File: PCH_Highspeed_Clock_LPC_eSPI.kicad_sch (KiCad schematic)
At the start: 1 part

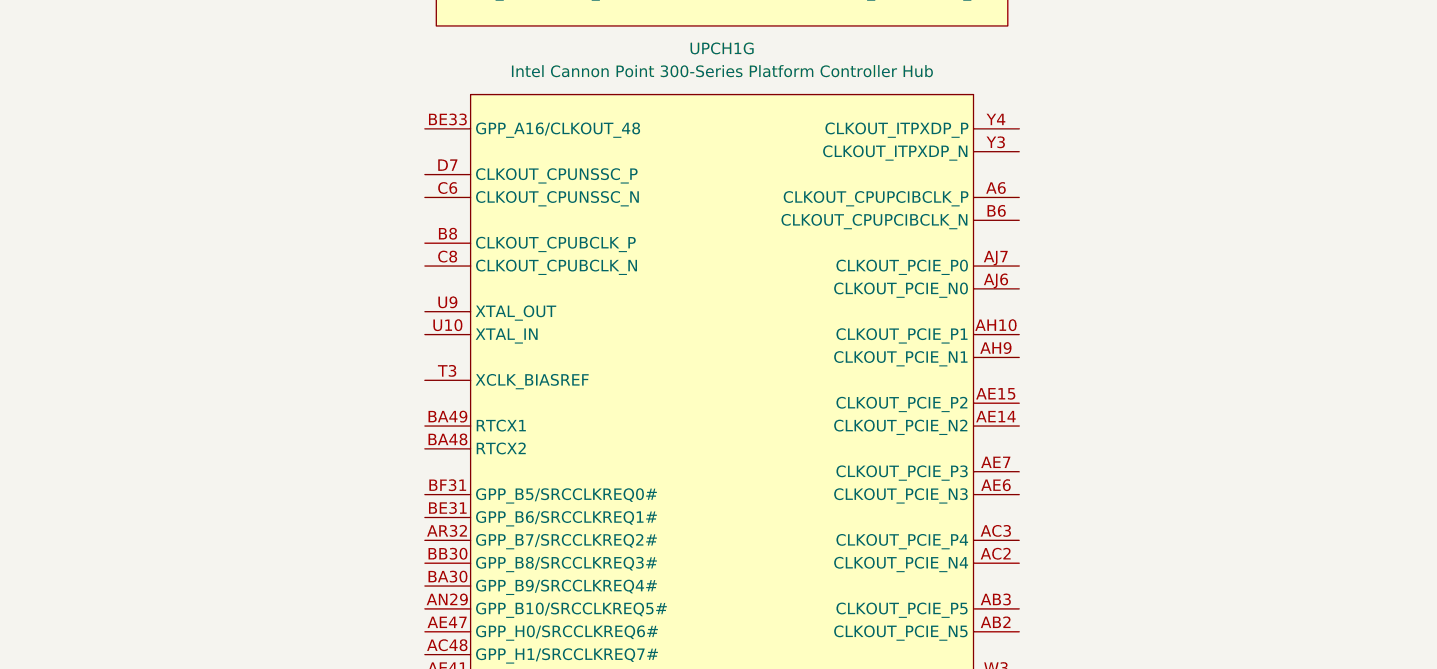
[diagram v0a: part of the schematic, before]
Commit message: Added pcie slot and cpu clocks
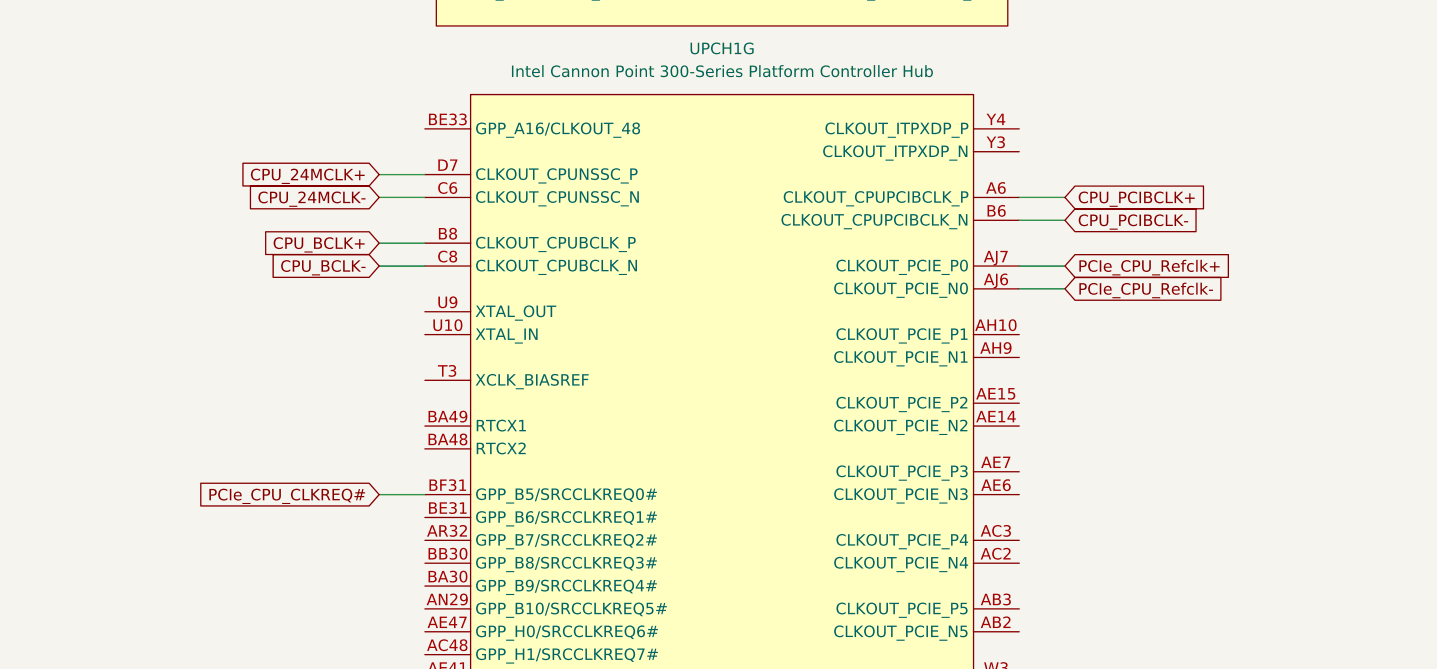
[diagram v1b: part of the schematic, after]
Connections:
- net CPU_PCIBCLK+: now reaches UPCH1.A6 (CLKOUT_CPUPCIBCLK_P)
- net PCIe_CPU_Refclk-: now reaches UPCH1.AJ6 (CLKOUT_PCIE_N0)
- net PCIe_CPU_Refclk+: now reaches UPCH1.AJ7 (CLKOUT_PCIE_P0)
- net CPU_PCIBCLK-: now reaches UPCH1.B6 (CLKOUT_CPUPCIBCLK_N)
- net CPU_BCLK+: now reaches UPCH1.B8 (CLKOUT_CPUBCLK_P)
- net PCIe_CPU_CLKREQ#: now reaches UPCH1.BF31 (GPP_B5/SRCCLKREQ0#)
- net CPU_24MCLK-: now reaches UPCH1.C6 (CLKOUT_CPUNSSC_N)
- net CPU_BCLK-: now reaches UPCH1.C8 (CLKOUT_CPUBCLK_N)
- net CPU_24MCLK+: now reaches UPCH1.D7 (CLKOUT_CPUNSSC_P)

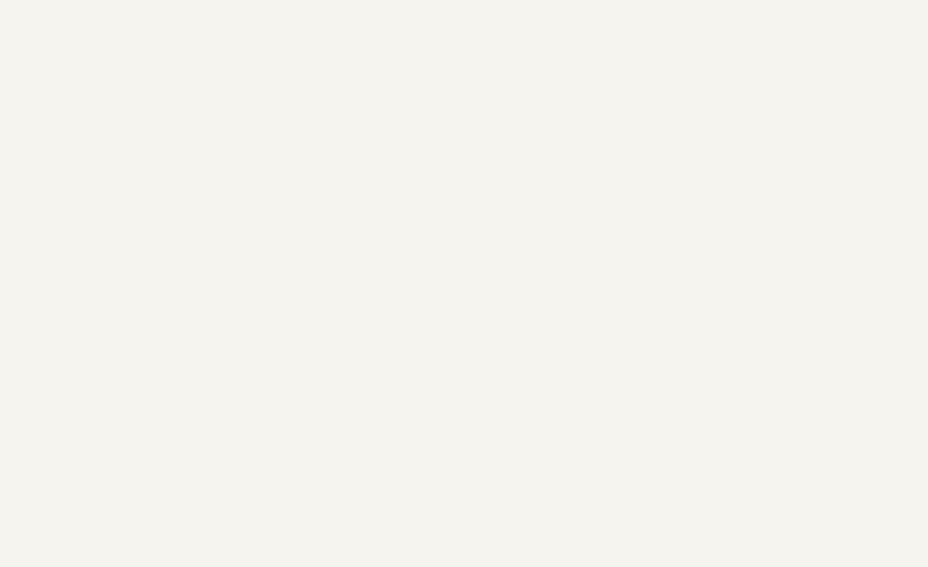
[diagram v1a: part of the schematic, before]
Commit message: Added PCH SKU IO table screenshot from datasheet to schematic
and a note about display audio
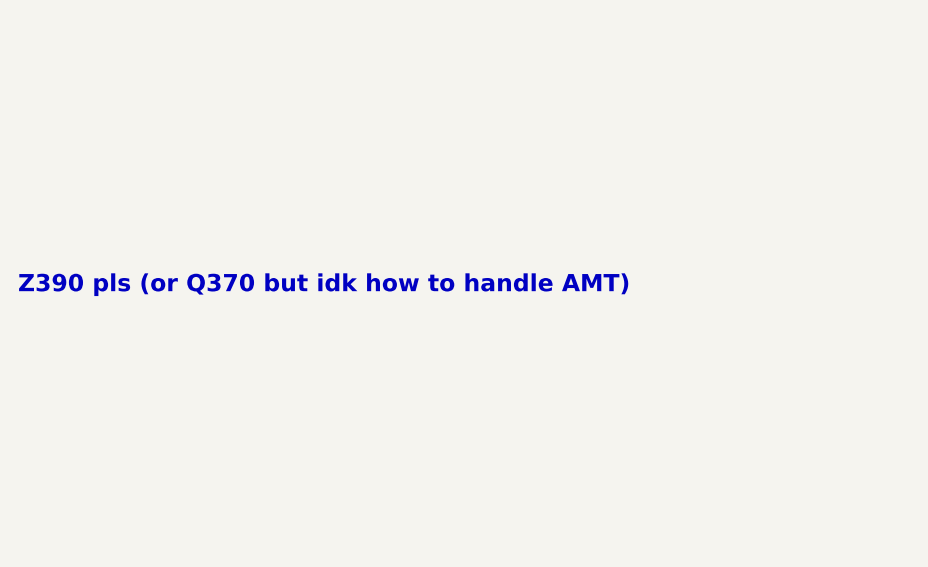
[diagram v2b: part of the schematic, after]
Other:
- note added: "Z390 pls (or Q370 but idk how to handle AMT)"

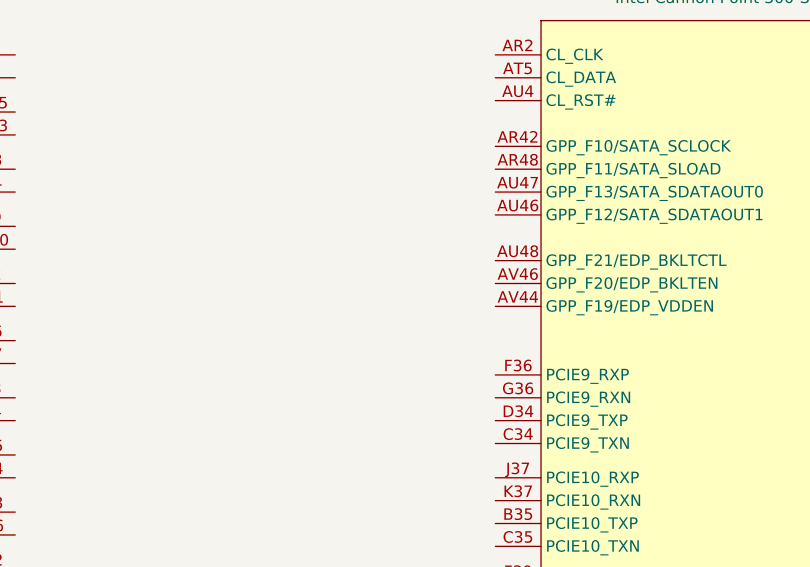
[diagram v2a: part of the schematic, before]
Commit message: partially added eDP + rearranged other display stuff
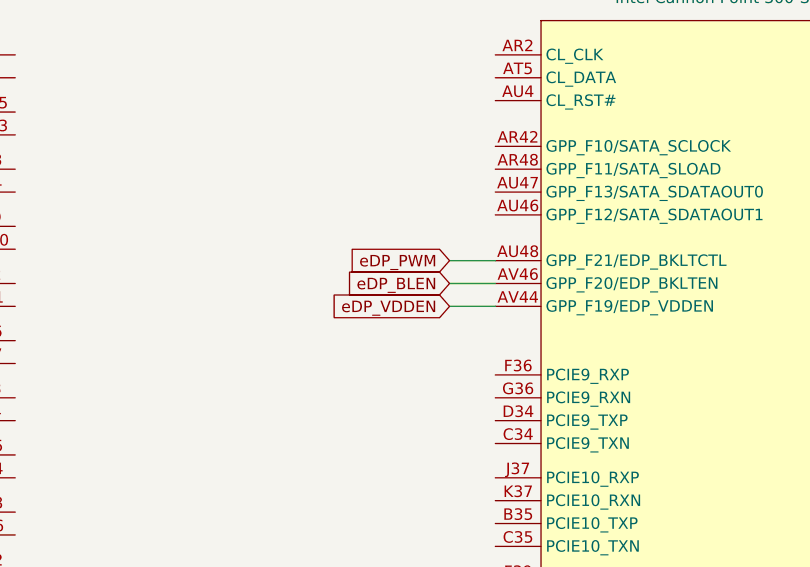
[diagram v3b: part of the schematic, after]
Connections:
- net eDP_PWM: now reaches UPCH1.AU48 (GPP_F21/EDP_BKLTCTL)
- net eDP_VDDEN: now reaches UPCH1.AV44 (GPP_F19/EDP_VDDEN)
- net eDP_BLEN: now reaches UPCH1.AV46 (GPP_F20/EDP_BKLTEN)
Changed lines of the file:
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@@
+	(wire
+		(pts
+			(xy 180.34 57.15) (xy 185.42 57.15)
+		)
+		(stroke
+			(width 0)
+			(type default)
+		)
+	)
 	(wire
 		(pts
@@
 	(wire
 		(pts
-			(xy 54.61 57.15) (xy 58.42 57.15)
+			(xy 180.34 52.07) (xy 185.42 52.07)
 		)
 		(stroke
@@
 	(wire
 		(pts
-			(xy 54.61 64.77) (xy 58.42 64.77)
+			(xy 54.61 57.15) (xy 58.42 57.15)
 		)
 		(stroke
@@
 	(wire
 		(pts
-			(xy 260.35 176.53) (xy 255.27 176.53)
+			(xy 54.61 64.77) (xy 58.42 64.77)
 		)
 		(stroke
@@
 	(wire
 		(pts
+			(xy 260.35 176.53) (xy 255.27 176.53)
+		)
+		(stroke
+			(width 0)
+			(type default)
+		)
+	)
+	(wire
+		(pts
 			(xy 184.15 176.53) (xy 189.23 176.53)
+		)
+		(stroke
+			(width 0)
+			(type default)
+		)
+	)
+	(wire
+		(pts
+			(xy 180.34 54.61) (xy 185.42 54.61)
 		)
 		(stroke
@@
 		)
 	)
+	(global_label "eDP_VDDEN"
+		(shape input)
+		(at 180.34 57.15 180)
+		(fields_autoplaced yes)
+		(effects
+			(font
+				(size 1.27 1.27)
+			)
+			(justify right)
+		)
+		(property "Intersheetrefs" "${INTERSHEET_REFS}"
+			(at 159.8771 57.15 0)
+			(effects
+				(font
+					(size 1.27 1.27)
+				)
+				(justify right)
+				(hide yes)
+			)
+		)
+	)
 	(global_label "DMI_CRx_PTx_2+"
 		(shape input)
@@
 		)
 	)
+	(global_label "eDP_PWM"
+		(shape input)
+		(at 180.34 52.07 180)
+		(fields_autoplaced yes)
+		(effects
+			(font
+				(size 1.27 1.27)
+			)
+			(justify right)
+		)
+		(property "Intersheetrefs" "${INTERSHEET_REFS}"
+			(at 159.8771 52.07 0)
+			(effects
+				(font
+					(size 1.27 1.27)
+				)
+				(justify right)
+				(hide yes)
+			)
+		)
+	)
 	(global_label "DMI_CTx_PRx_2+"
 		(shape input)
@@
 			(effects
 				(font
+					(size 1.27 1.27)
+				)
+				(justify right)
+				(hide yes)
+			)
+		)
+	)
+	(global_label "eDP_BLEN"
+		(shape input)
+		(at 180.34 54.61 180)
+		(fields_autoplaced yes)
+		(effects
+			(font
+				(size 1.27 1.27)
+			)
+			(justify right)
+		)
+		(property "Intersheetrefs" "${INTERSHEET_REFS}"
+			(at 159.8771 54.61 0)
+			(effects
+				(font

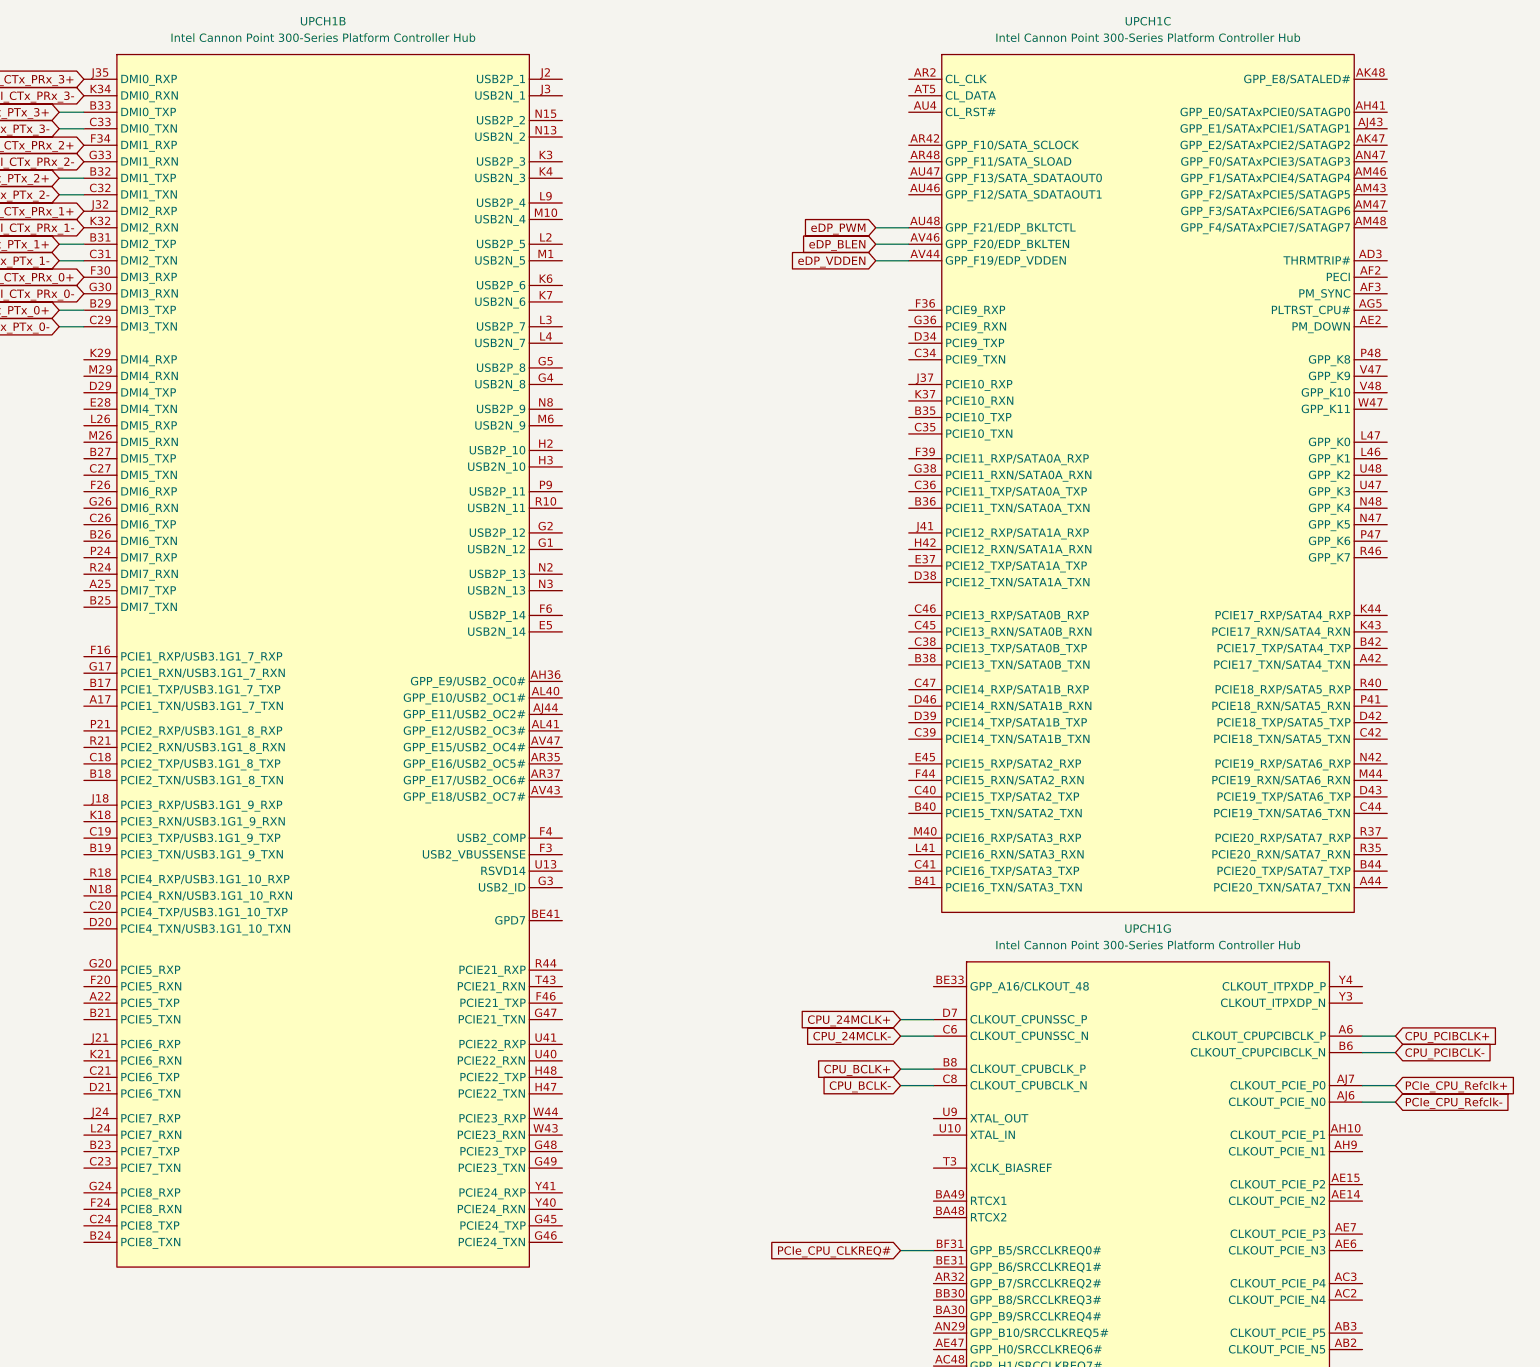
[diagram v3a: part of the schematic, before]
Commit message: Added PCH PCIe rootport/bifurcation notes
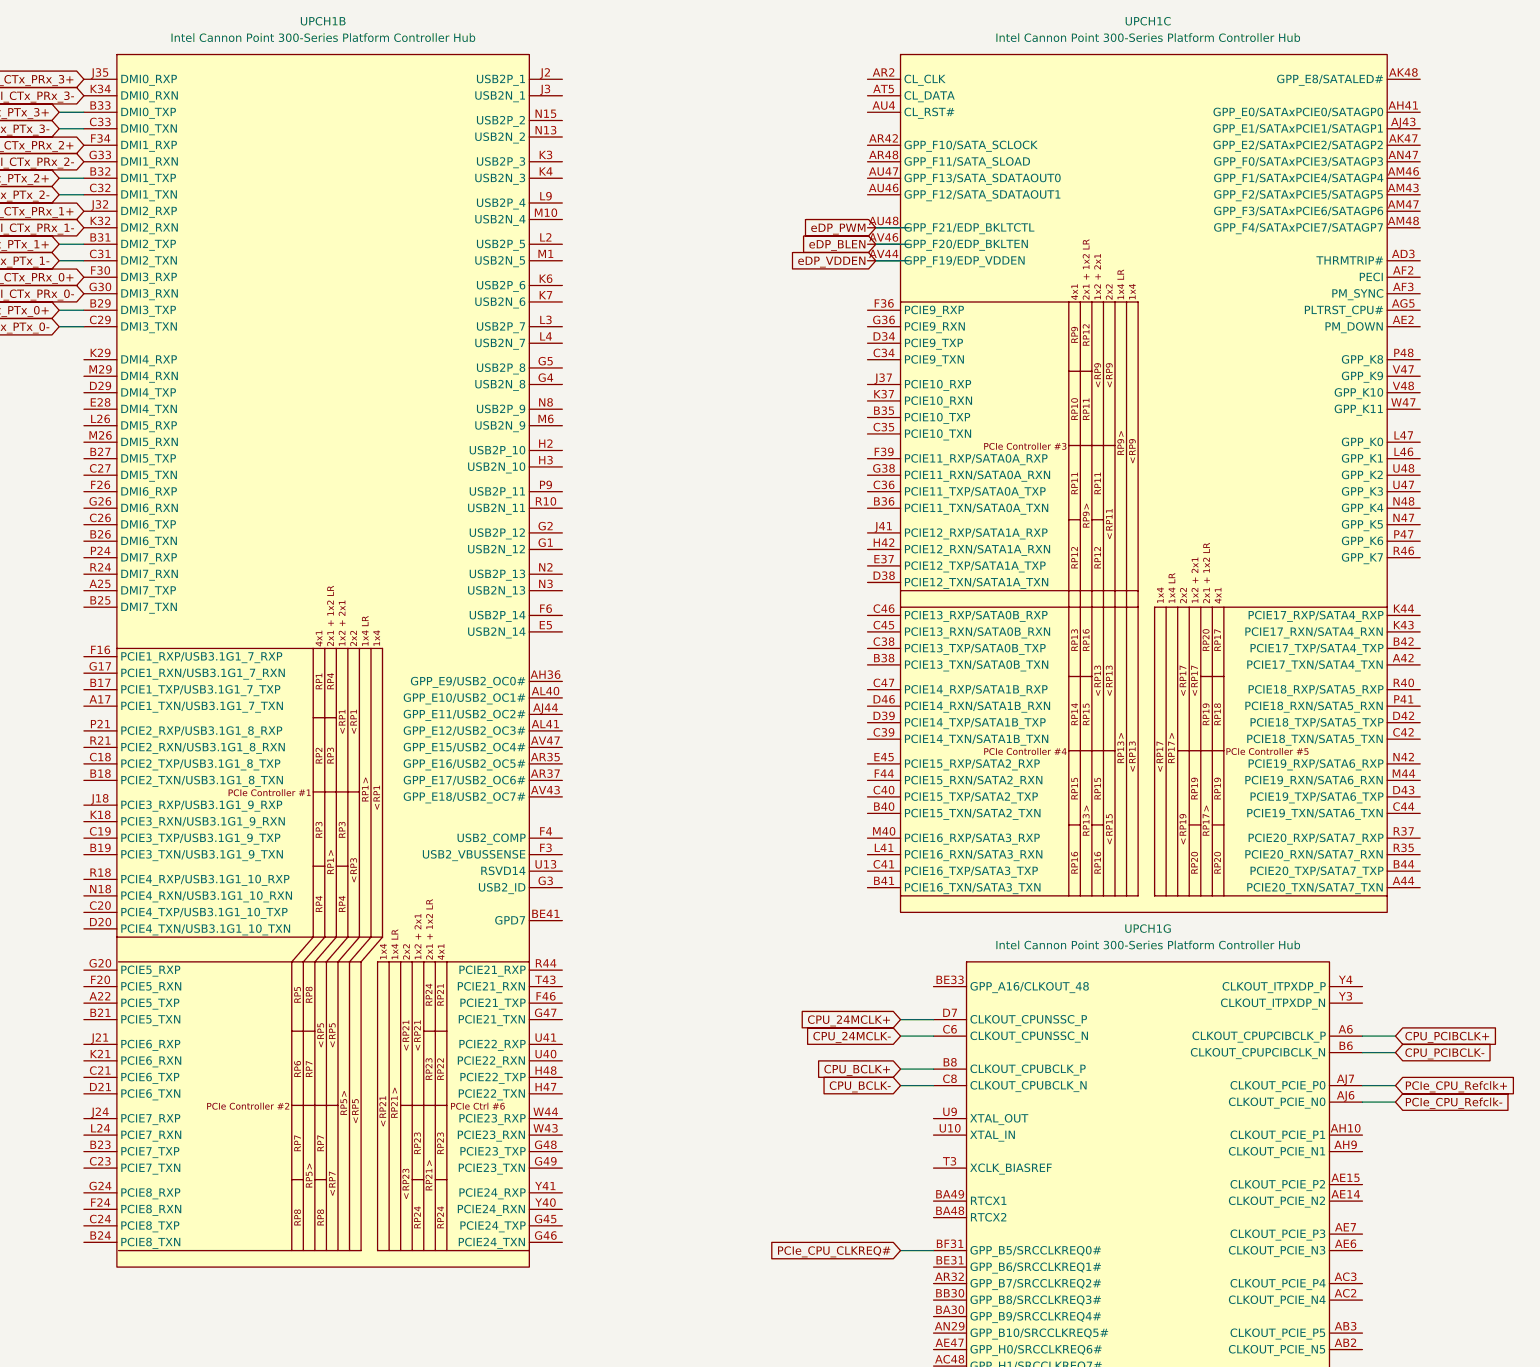
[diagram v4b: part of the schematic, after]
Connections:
- net eDP_BLEN: no longer UPCH1.AV46 (GPP_F20/EDP_BKLTEN)
- net eDP_PWM: no longer UPCH1.AU48 (GPP_F21/EDP_BKLTCTL)
- net eDP_VDDEN: no longer UPCH1.AV44 (GPP_F19/EDP_VDDEN)
